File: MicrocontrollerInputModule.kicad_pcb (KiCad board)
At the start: 2 copper layers, 31 x 111.4 mm, 369 parts, among them J2 FH34SRJ-12S-0.5SH_50_, SW3 A6H-2101, U1 W25Q16JVUXIQ, U2 RP2040, U3 74AHC125BQ_115, U4 74AHC125BQ_115, Y1 12.000MHz

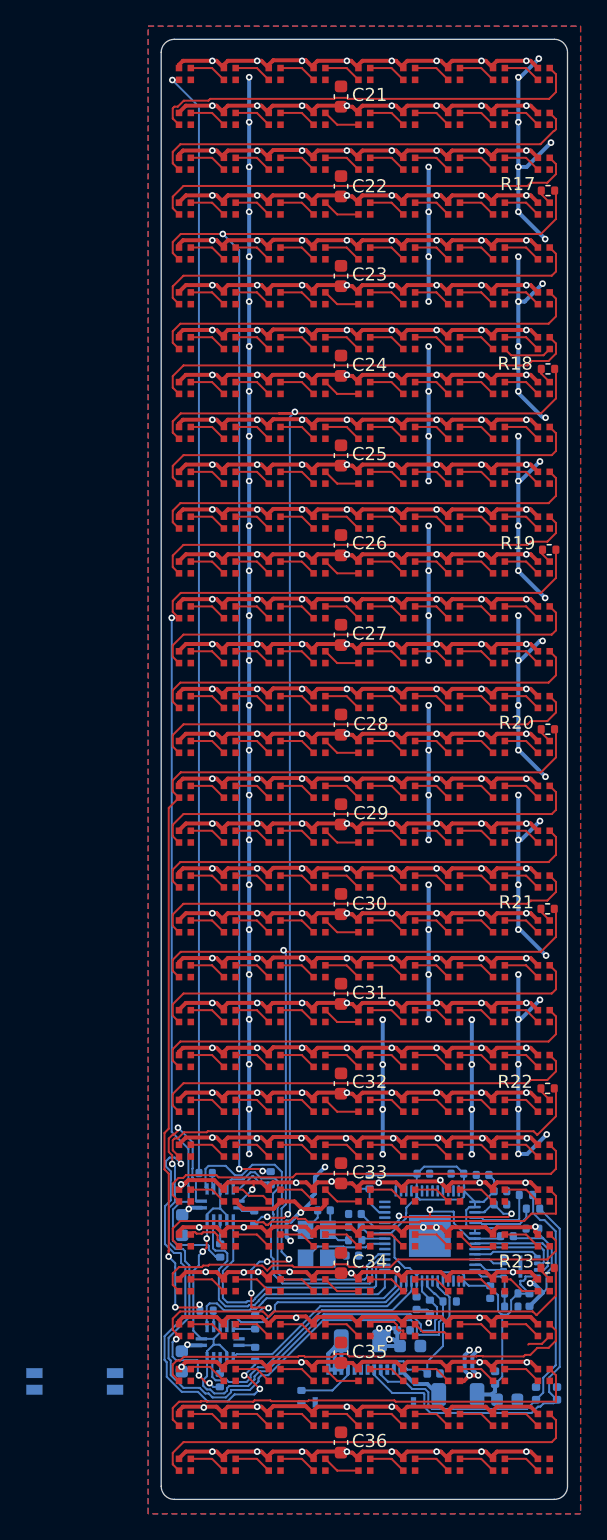
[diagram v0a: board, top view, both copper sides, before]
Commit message: Arya Edits and Feedback plus DIP Switch
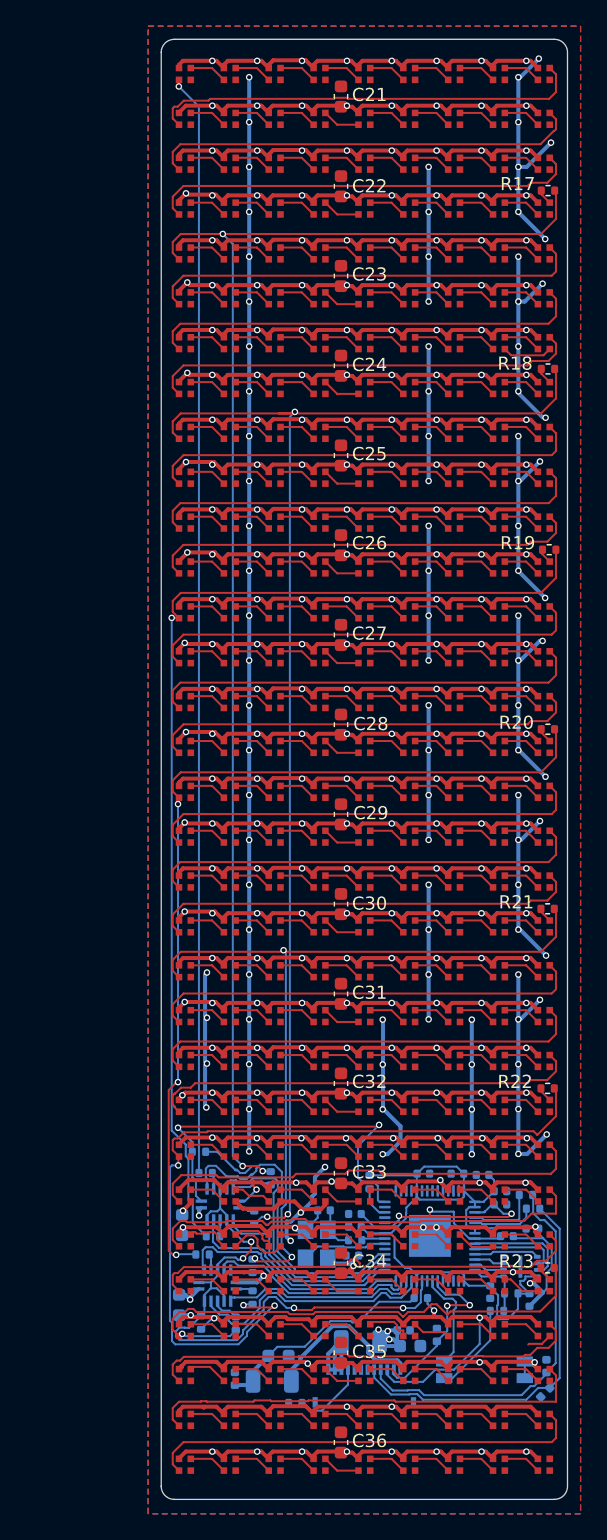
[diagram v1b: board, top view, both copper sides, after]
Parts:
- moved SW3 31.3 mm to (55.3, 119.6), turned to 180 degrees
- moved R24 22.3 mm to (33.5, 102.9)
- moved D1 19.9 mm to (36.2, 120.2)
- moved C16 17.8 mm to (39.6, 118.5)
- moved R8 17.5 mm to (33.6, 116.0)
- moved F2 14.2 mm to (39.1, 120.4), turned to 180 degrees
- moved R16 4.49 mm to (36.3, 116.0)
- moved U4 4.31 mm to (34.9, 113.1)
- moved C18 4.31 mm to (32.0, 114.6)
- moved R14 4.31 mm to (37.6, 111.6)
- moved R15 4.31 mm to (37.6, 114.1)
- moved R13 4.29 mm to (33.8, 110.8)
- moved D5 2.96 mm to (51.6, 116.9), turned to -90 degrees
- moved D4 2.23 mm to (60.0, 119.3)
- moved R12 1.22 mm to (34.6, 109.4), turned to 180 degrees
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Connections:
- R24 pad 2: Net-(U2-GPIO6) -> /~{OE1}
- SW3 pad 3: ~{RESET} -> BOOTSEL
- SW3 pad 4: BOOTSEL -> /~{DEBUG}
- U2 pad 28: unconnected-(U2-GPIO17-Pad28) -> /~{OE1}
- U2 pad 7: unconnected-(U2-GPIO5-Pad7) -> /~{DEBUG}
- U2 pad 8: Net-(U2-GPIO6) -> unconnected-(U2-GPIO6-Pad8)
- U3 pad 1: Net-(U2-GPIO6) -> /~{OE1}
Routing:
- net Net-(U2-GPIO6): track 57.4 -> 0.00 mm, vias 2 -> 0
- net /~{OE1}: track 0.00 -> 29.9 mm, vias 0 -> 2
- net GND: track 1051.6 -> 1077.5 mm, vias 241 -> 243
- net +5V: track 293.8 -> 303.6 mm, vias 103 -> 104
- net +3V3: track 62.9 -> 72.5 mm
- net Net-(F2-Pad1): track 3.71 -> 12.7 mm
- net /~{DEBUG}: track 0.00 -> 7.63 mm
- net BOOTSEL: track 0.00 -> 6.95 mm
- net /D13: track 20.8 -> 15.1 mm
- net /NeopixelMatrix/STRIP11: track 66.5 -> 61.1 mm, vias 5 -> 3
- net /D12: track 22.1 -> 16.9 mm
- net /NeopixelMatrix/STRIP7: track 87.5 -> 82.5 mm
- net /NeopixelMatrix/STRIP9: track 75.8 -> 71.0 mm
- net /NeopixelMatrix/STRIP13: track 65.8 -> 61.1 mm
- net /D7: track 47.4 -> 43.6 mm, vias 2 -> 4
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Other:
- board text removed: "BOOT"
- board text removed: "RESET"

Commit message: Adjusting silk screen and some wires
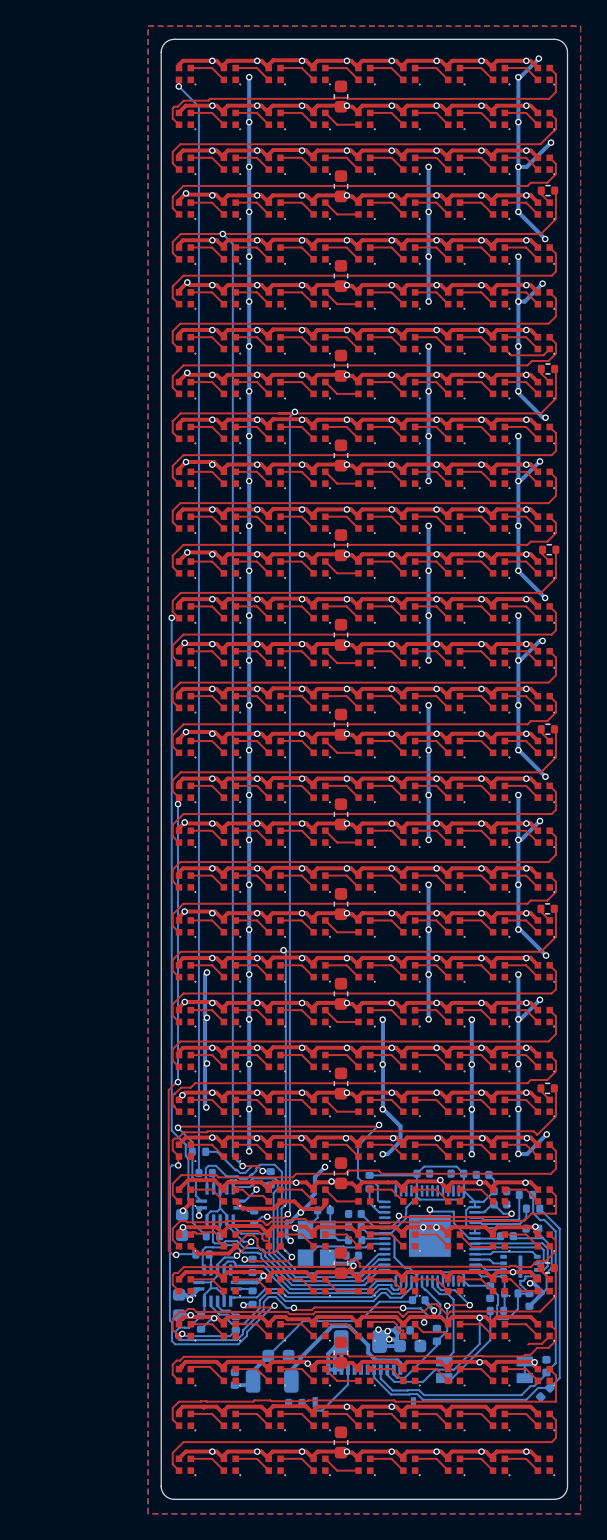
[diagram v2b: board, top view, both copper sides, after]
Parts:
- moved C12 0.22 mm to (50.3, 114.2)
- renumbered SW3 to SW1
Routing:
- net +5V: track 303.6 -> 307.5 mm
- net /D7: track 43.6 -> 46.2 mm
- net /NeopixelMatrix/STRIP11: track 61.1 -> 62.2 mm
- net GND: track 1077.5 -> 1077.8 mm, vias 243 -> 244
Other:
- board text added: "Arya and Nirav"
- board text added: "LED Strip | GPIO 1 Top | D15 2 | D14 3 | D13 4 | D12"
- board text added: "LED Strip | GPIO 5 | D11 6 | D10 7 | D9 8 Bot | D8"
- board text added: "Thank you so much for all of your help and encouragement. I couldn't have done this without you."
- board text removed: "LED Strip | GPIO Pin 1 Top | D15 2 | D14 3 | D13 4 | D12 5 | D11 6 | D10 7 | D9 8 Bot | D8"

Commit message: Fabrication edits
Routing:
- net GND: track 1077.8 -> 1077.7 mm, vias 244 -> 246
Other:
- board text added: "Thank you so much Arya and Nirav for all of your help and encouragement. I couldn't have done this without you."
- board text removed: "Arya and Nirav"
- board text removed: "Thank you so much for all of your help and encouragement. I couldn't have done this without you."

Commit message: V3 update in preparation for sale
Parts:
- removed C21, C22, C23, C24, C25, C26, C27, C28, C29, C30, C31, C32, C33, C34, C35, C36: 10uF, Capacitor_SMD:C_0603_1608Metric
- removed R17, R18, R19, R20, R21, R22, R23: 0, Resistor_SMD:R_0402_1005Metric
- added ?: , , F.Cu at (35.2, 28.1)
- added ?: , , F.Cu at (56.5, 28.1)
- added ?: , , F.Cu at (56.3, 60.8)
- added REF**: TestPoint_Pad_2.0x2.0mm, TestPoint:TestPoint_Pad_2.0x2.0mm, B.Cu at (59.7, 126.1)
- added REF**: TestPoint_Pad_1.5x1.5mm, TestPoint:TestPoint_Pad_1.5x1.5mm, B.Cu at (34.8, 60.8)
- added REF**: TestPoint_Pad_2.0x2.0mm, TestPoint:TestPoint_Pad_2.0x2.0mm, B.Cu at (32.3, 126.1)
- N1, N10, N100, N101, N102, N103, N104, N105, N106, N107, N108, N109, N11, N110, N111, N112, N113, N114, N115, N116, N117, N118, N119, N12, N120, N121, N122, N123, N124, N125, N126, N127, N128, N129, N13, N130, N131, N132, N133, N134, N135, N136, N137, N138, N139, N14, N140, N141, N142, N143, N144, N145, N146, N147, N148, N149, N15, N150, N151, N152, N153, N154, N155, N156, N157, N158, N159, N16, N160, N161, N162, N163, N164, N165, N166, N167, N168, N169, N17, N170, N171, N172, N173, N174, N175, N176, N177, N178, N179, N18, N180, N181, N182, N183, N184, N185, N186, N187, N188, N189, N19, N190, N191, N192, N193, N194, N195, N196, N197, N198, N199, N2, N20, N200, N201, N202, N203, N204, N205, N206, N207, N208, N209, N21, N210, N211, N212, N213, N214, N215, N216, N217, N218, N219, N22, N220, N221, N222, N223, N224, N225, N226, N227, N228, N229, N23, N230, N231, N232, N233, N234, N235, N236, N237, N238, N239, N24, N240, N241, N242, N243, N244, N245, N246, N247, N248, N249, N25, N250, N251, N252, N253, N254, N255, N256, N257, N258, N259, N26, N260, N261, N262, N263, N264, N265, N266, N267, N268, N269, N27, N270, N271, N272, N273, N274, N275, N276, N277, N278, N279, N28, N280, N281, N282, N283, N284, N285, N286, N287, N288, N29, N3, N30, N31, N32, N33, N34, N35, N36, N37, N38, N39, N4, N40, N41, N42, N43, N44, N45, N46, N47, N48, N49, N5, N50, N51, N52, N53, N54, N55, N56, N57, N58, N59, N6, N60, N61, N62, N63, N64, N65, N66, N67, N68, N69, N7, N70, N71, N72, N73, N74, N75, N76, N77, N78, N79, N8, N80, N81, N82, N83, N84, N85, N86, N87, N88, N89, N9, N90, N91, N92, N93, N94, N95, N96, N97, N98, N99: value ~ -> SK6805-EC14
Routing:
- net /NeopixelMatrix/STRIP15: track 39.0 -> 4.34 mm
- net /NeopixelMatrix/STRIP9: track 71.0 -> 37.3 mm
- net /NeopixelMatrix/STRIP7: track 82.5 -> 48.8 mm
- net /NeopixelMatrix/STRIP13: track 61.1 -> 27.5 mm
- net /NeopixelMatrix/STRIP3: track 107.5 -> 79.4 mm
- net /NeopixelMatrix/STRIP5: track 99.3 -> 75.5 mm
- net /NeopixelMatrix/STRIP11: track 62.2 -> 38.7 mm
- net /~{OE1}: track 29.9 -> 26.3 mm
- net /NeopixelMatrix/END-STRIP8: track 1.18 -> 0.00 mm
- net /NeopixelMatrix/END-STRIP12: track 1.18 -> 0.00 mm
- net /NeopixelMatrix/END-STRIP2: track 1.18 -> 0.00 mm
- net /NeopixelMatrix/END-STRIP6: track 1.18 -> 0.00 mm
- net /NeopixelMatrix/END-STRIP4: track 1.18 -> 0.00 mm
- net /NeopixelMatrix/END-STRIP14: track 1.18 -> 0.00 mm
- net /NeopixelMatrix/END-STRIP10: track 1.18 -> 0.00 mm
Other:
- board text added: "by Joe Schroedl, v3"
- board text added: "https://jschroedl.com"
- board text removed: "by Joe Schroedl, v2"
- board text removed: "https://github.com/corndog2000"
